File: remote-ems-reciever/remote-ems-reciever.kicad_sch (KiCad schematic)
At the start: 36 parts, among them IC1 Wio-E5, IC2 MCP2562, J1 Conn_Coaxial, J2 Conn_01x04, J3 Conn_01x04, J4 Conn_01x04_Pin, J5 Conn_01x04, Q1 BSS138, SW1 SW_Push, SW2 SW_Push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

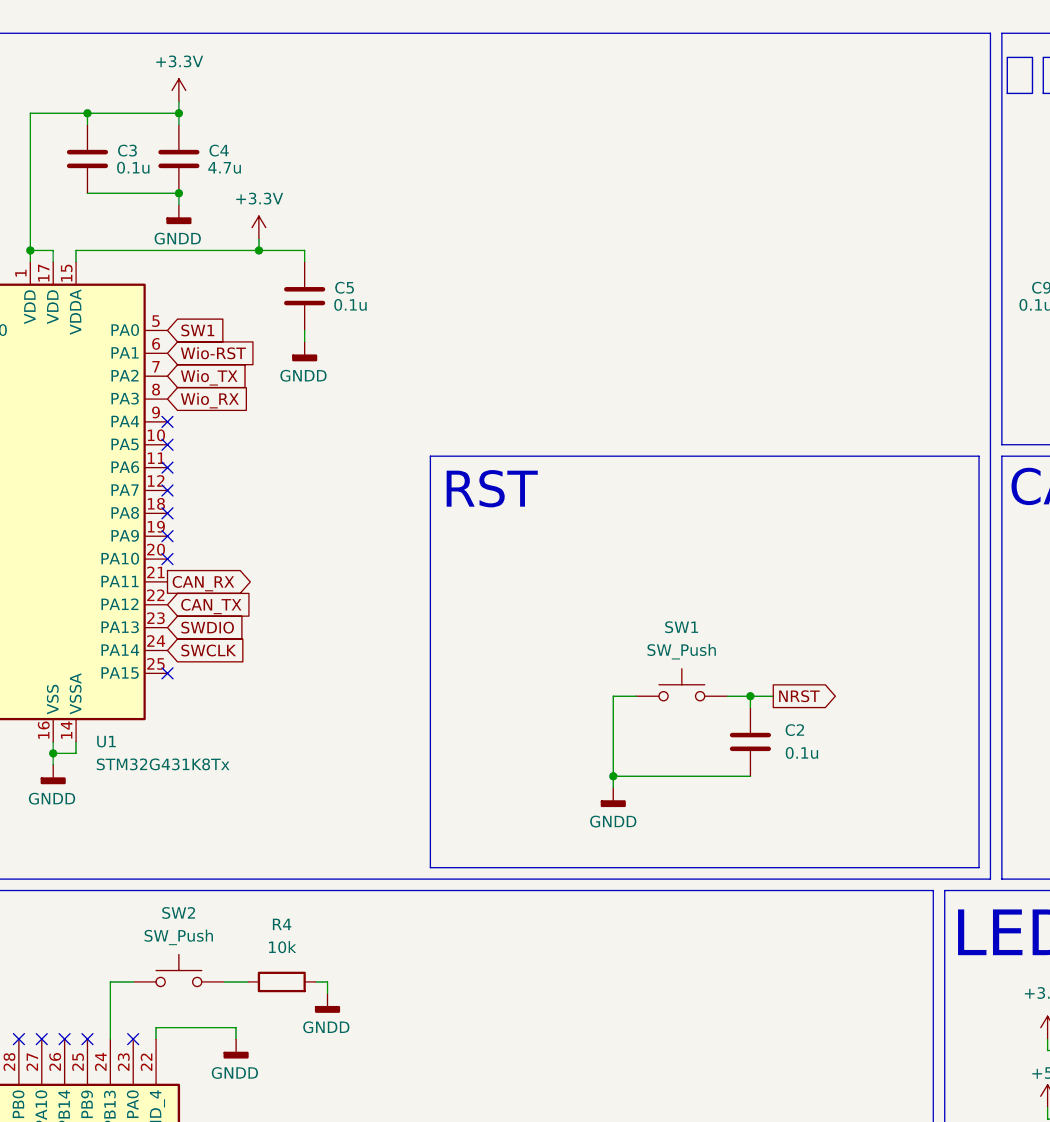
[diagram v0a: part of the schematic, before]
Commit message: remote-ems-transmitter　ビア、シルク、LED以外完成
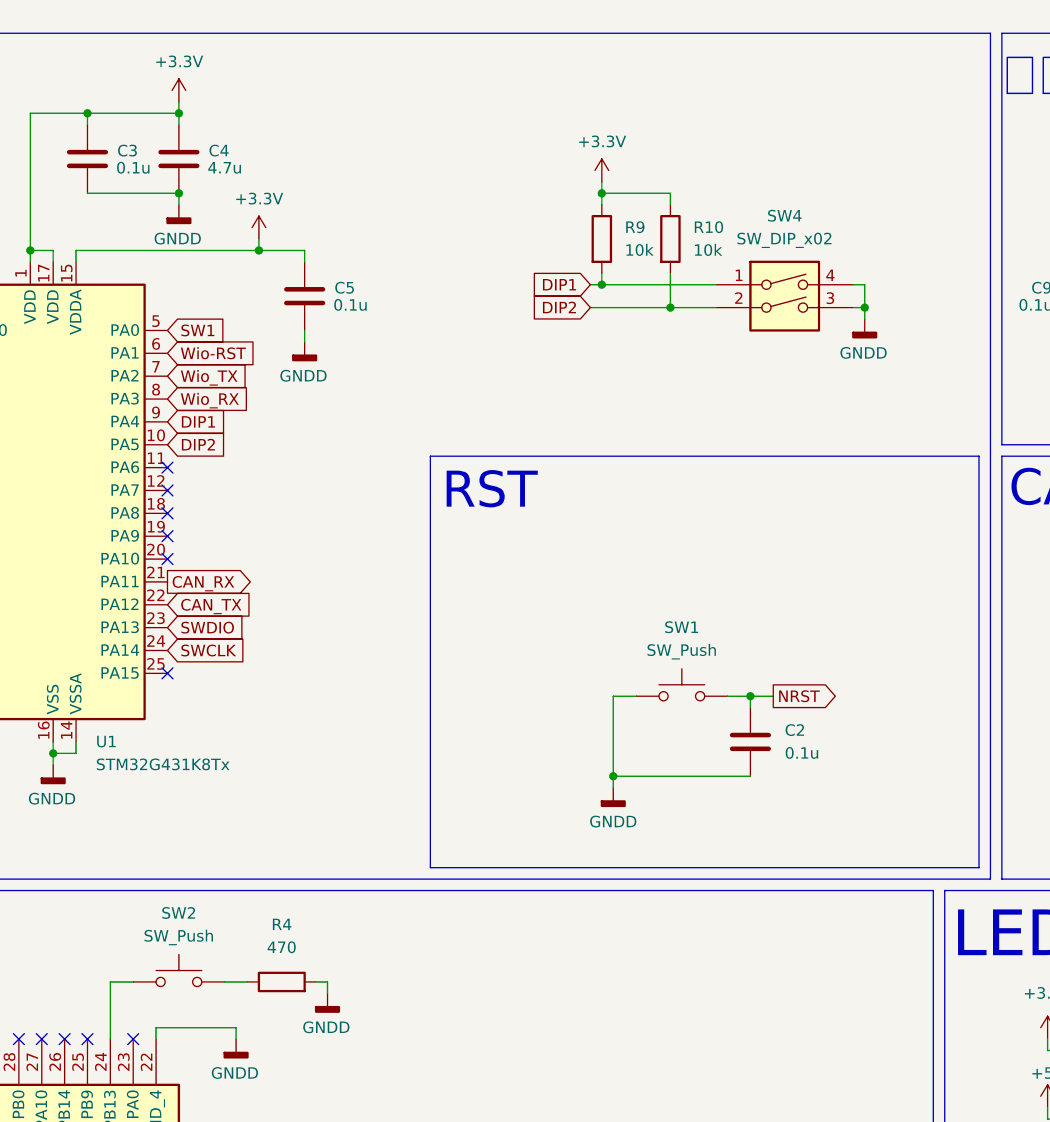
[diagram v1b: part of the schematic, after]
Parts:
- added R10, R9: 10k, Resistor_SMD:R_0603_1608Metric_Pad0.98x0.95mm_HandSolder, symbol Device:R
- added SW4: SW_DIP_x02, Button_Switch_THT:SW_DIP_SPSTx02_Slide_9.78x7.26mm_W7.62mm_P2.54mm, symbol Switch:SW_DIP_x02
- R4: value 10k -> 470
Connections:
- net +3.3V: now also R10.1, R9.1
- net GNDD: now also SW4.3, SW4.4
- net DIP2: now reaches U1.10 (PA5)
- net DIP2: now also R10.2, SW4.2
- net DIP1: now reaches U1.9 (PA4)
- net DIP1: now also R9.2, SW4.1
- no-connect marks 31 -> 29

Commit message: remote-ems-reciever　ビア、シルク、LED以外完成
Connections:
- net DIP1: now also U1.27 (PB4); no longer U1.9 (PA4)
- net DIP2: now also U1.28 (PB5); no longer U1.10 (PA5)
- net LED1: now also U1.26 (PB3); no longer U1.27 (PB4)
- net LED2: now also U1.25 (PA15); no longer U1.28 (PB5)
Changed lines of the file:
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@@
+	)
+	(no_connect
+		(at 63.5 55.88)
 	)
 	(no_connect
@@
 	)
 	(no_connect
-		(at 63.5 83.82)
-	)
-	(no_connect
 		(at 38.1 50.8)
 	)
@@
 	)
 	(no_connect
-		(at 38.1 60.96)
-	)
-	(no_connect
 		(at 39.37 152.4)
 	)
@@
 	(no_connect
 		(at 69.85 149.86)
+	)
+	(no_connect
+		(at 63.5 58.42)
 	)
 	(no_connect
@@
 	(global_label "DIP1"
 		(shape input)
-		(at 63.5 55.88 0)
+		(at 38.1 63.5 180)
+		(fields_autoplaced yes)
+		(effects
+			(font
+				(size 1.27 1.27)
+			)
+			(justify right)
+		)
+		(property "Intersheetrefs" "${INTERSHEET_REFS}"
+			(at 30.7605 63.5 0)
+			(effects
+				(font
+					(size 1.27 1.27)
+				)
+				(justify right)
+				(hide yes)
+			)
+		)
+	)
+	(global_label "SWCLK"
+		(shape input)
+		(at 245.872 31.75 0)
 		(fields_autoplaced yes)
 		(effects
@@
 		)
 		(property "Intersheetrefs" "${INTERSHEET_REFS}"
-			(at 70.8395 55.88 0)
+			(at 255.0862 31.75 0)
 			(effects
 				(font
@@
 		)
 	)
-	(global_label "SWCLK"
-		(shape input)
-		(at 245.872 31.75 0)
-		(fields_autoplaced yes)
-		(effects
-			(font
-				(size 1.27 1.27)
-			)
-			(justify left)
-		)
-		(property "Intersheetrefs" "${INTERSHEET_REFS}"
-			(at 255.0862 31.75 0)
-			(effects
-				(font
-					(size 1.27 1.27)
-				)
-				(justify left)
-				(hide yes)
-			)
-		)
-	)
 	(global_label "LED2"
 		(shape input)
@@
 	(global_label "LED1"
 		(shape input)
-		(at 38.1 63.5 180)
+		(at 38.1 60.96 180)
 		(fields_autoplaced yes)
 		(effects
@@
 		)
 		(property "Intersheetrefs" "${INTERSHEET_REFS}"
-			(at 30.4582 63.5 0)
+			(at 30.4582 60.96 0)
 			(effects
 				(font
@@
 	(global_label "LED2"
 		(shape input)
+		(at 63.5 83.82 0)
+		(fields_autoplaced yes)
+		(effects
+			(font
+				(size 1.27 1.27)
+			)
+			(justify left)
+		)
+		(property "Intersheetrefs" "${INTERSHEET_REFS}"
+			(at 71.1418 83.82 0)
+			(effects
+				(font
+					(size 1.27 1.27)
+				)
+				(justify left)
+				(hide yes)
+			)
+		)
+	)
+	(global_label "LED1"
+		(shape input)
+		(at 161.29 140.97 180)
+		(fields_autoplaced yes)
+		(effects
+			(font
+				(size 1.27 1.27)
+			)
+			(justify right)
+		)
+		(property "Intersheetrefs" "${INTERSHEET_REFS}"
+			(at 153.6482 140.97 0)
+			(effects
+				(font
+					(size 1.27 1.27)
+				)
+				(justify right)
+				(hide yes)
+			)
+		)
+	)
+	(global_label "DIP2"
+		(shape input)
 		(at 38.1 66.04 180)
 		(fields_autoplaced yes)
@@
 		)
 		(property "Intersheetrefs" "${INTERSHEET_REFS}"
-			(at 30.4582 66.04 0)
+			(at 30.7605 66.04 0)
 			(effects
 				(font
@@
 				(hide yes)
 			)
-		)
-	)
-	(global_label "LED1"
-		(shape input)
-		(at 161.29 140.97 180)
-		(fields_autoplaced yes)
-		(effects
-			(font
-				(size 1.27 1.27)
-			)
-			(justify right)
-		)
-		(property "Intersheetrefs" "${INTERSHEET_REFS}"
-			(at 153.6482 140.97 0)
-			(effects
-				(font
-					(size 1.27 1.27)
-				)
-				(justify right)
-				(hide yes)
-			)
-		)
-	)
-	(global_label "DIP2"
-		(shape input)
-		(at 63.5 58.42 0)
-		(fields_autoplaced yes)
-		(effects
-			(font
-				(size 1.27 1.27)
-			)
-			(justify left)
-		)
-		(property "Intersheetrefs" "${INTERSHEET_REFS}"
-			(at 70.8395 58.42 0)
-			(effects
-				(font
-					(size 1.27 1.27)
-				)
-				(justify left)
-				(hide yes)
-			)

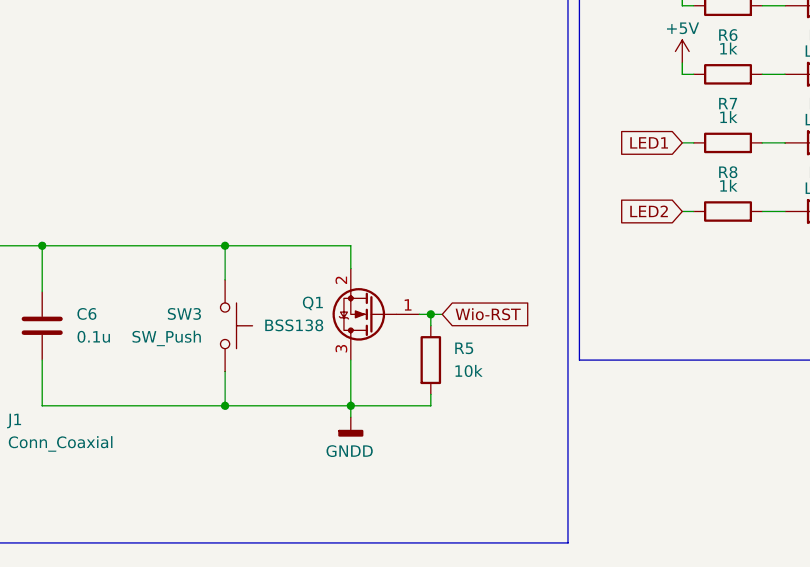
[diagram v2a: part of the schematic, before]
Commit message: FETの向きを修正 ガーバー出力
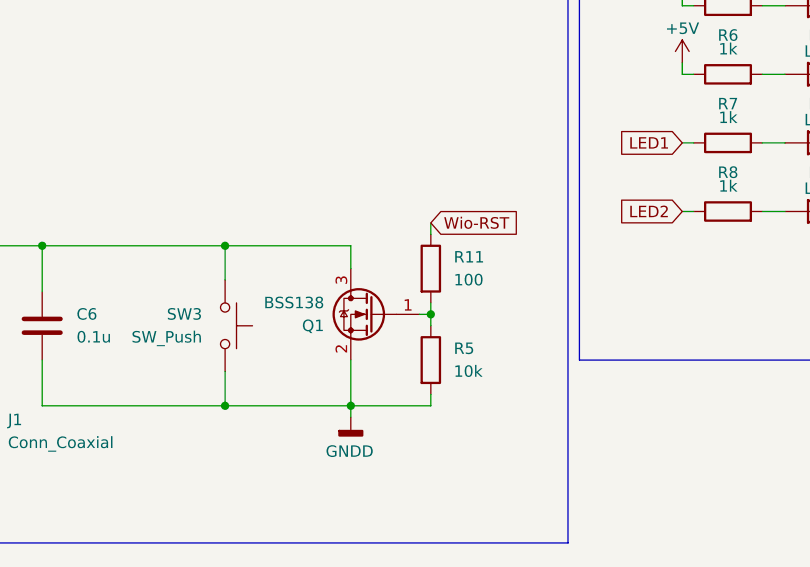
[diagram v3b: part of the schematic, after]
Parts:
- added R11: 100, Resistor_SMD:R_0603_1608Metric_Pad0.98x0.95mm_HandSolder, symbol Device:R
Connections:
- net GNDD: now also Q1.2 (S); no longer Q1.3 (D)
- net Wio-RST: now also R11.1; no longer Q1.1 (G), R5.1
- net at C6.1, IC1.17 (RST), SW3.2: now also Q1.3 (D); no longer Q1.2 (S)
- new net: Q1.1 (G), R11.2, R5.1
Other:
- moved on the sheet: Q1
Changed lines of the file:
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@@
 	)
 	(junction
-		(at 133.35 160.02)
-		(diameter 0)
-		(color 0 0 0 0)
-	)
-	(junction
 		(at 243.586 73.66)
 		(diameter 0)
@@
 	)
 	(junction
+		(at 133.35 160.02)
+		(diameter 0)
+		(color 0 0 0 0)
+	)
+	(junction
 		(at 64.77 21.59)
 		(diameter 0)
@@
 	(wire
 		(pts
+			(xy 133.35 149.86) (xy 133.35 151.13)
+		)
+		(stroke
+			(width 0)
+			(type default)
+		)
+	)
+	(wire
+		(pts
 			(xy 265.43 29.21) (xy 267.97 29.21)
 		)
@@
 	(wire
 		(pts
-			(xy 134.62 160.02) (xy 133.35 160.02)
-		)
-		(stroke
-			(width 0)
-			(type default)
-		)
-	)
-	(wire
-		(pts
 			(xy 218.44 83.82) (xy 234.95 83.82)
 		)
@@
 	(wire
 		(pts
+			(xy 133.35 158.75) (xy 133.35 160.02)
+		)
+		(stroke
+			(width 0)
+			(type default)
+		)
+	)
+	(wire
+		(pts
 			(xy 50.8 93.98) (xy 50.8 92.71)
 		)
@@
 	(global_label "Wio-RST"
 		(shape input)
-		(at 134.62 160.02 0)
+		(at 133.35 149.86 0)
 		(fields_autoplaced yes)
 		(effects
@@
 		)
 		(property "Intersheetrefs" "${INTERSHEET_REFS}"
-			(at 145.8299 160.02 0)
+			(at 144.5599 149.86 0)
 			(effects
 				(font
@@
 	)
 	(symbol
+		(lib_id "Device:R")
+		(at 133.35 154.94 0)
+		(unit 1)
+		(exclude_from_sim no)
+		(in_bom yes)
+		(on_board yes)
+		(dnp no)
+		(fields_autoplaced yes)
+		(property "Reference" "R11"
+			(at 135.89 153.6699 0)
+			(effects
+				(font
+					(size 1.27 1.27)
+				)
+				(justify left)
+			)
+		)
+		(property "Value" "100"
+			(at 135.89 156.2099 0)
+			(effects
+				(font
+					(size 1.27 1.27)
+				)
+				(justify left)
+			)
+		)
+		(property "Footprint" "Resistor_SMD:R_0603_1608Metric_Pad0.98x0.95mm_HandSolder"
+			(at 131.572 154.94 90)
+			(effects
+				(font
+					(size 1.27 1.27)
+				)
+				(hide yes)
+			)
+		)
+		(property "Datasheet" "~"
+			(at 133.35 154.94 0)
+			(effects
+				(font
+					(size 1.27 1.27)
+				)
+				(hide yes)
+			)
+		)
+		(property "Description" ""
+			(at 133.35 154.94 0)
+			(effects
+				(font
+					(size 1.27 1.27)
+				)
+				(hide yes)
+			)
+		)
+		(pin "1"
+		)
+		(pin "2"
+		)
+		(instances
+			(project "remote-ems-reciever"
+				(path "/279d1b04-8b37-430e-b98e-03e2207b8b9f"
+					(reference "R11")
+					(unit 1)
+				)
+			)
+		)
+	)
+	(symbol
 		(lib_id "Connector_Generic:Conn_01x04")
 		(at 209.677 27.94 0)
@@
 	(symbol
 		(lib_id "Transistor_FET:BSS138")
-		(at 127 160.02 180)
+		(at 127 160.02 0)
+		(mirror y)
 		(unit 1)
 		(exclude_from_sim no)
@@
 		(dnp no)
 		(property "Reference" "Q1"
-			(at 121.5136 158.7499 0)
+			(at 121.5136 161.2901 0)
 			(effects
 				(font
@@
 		)
 		(property "Value" "BSS138"
-			(at 121.5136 161.2899 0)
+			(at 121.5136 158.7501 0)
 			(effects
 				(font
@@
 		)
 		(property "Footprint" "Package_TO_SOT_SMD:SOT-23"
-			(at 121.92 158.115 0)
+			(at 121.92 161.925 0)
 			(effects
 				(font
